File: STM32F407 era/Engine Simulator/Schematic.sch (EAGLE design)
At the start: 23 parts, among them U1 MAX13052ESA+, U2 AD5293BRUZ-100, U3 AD5024BRUZ, X4 057-006-1

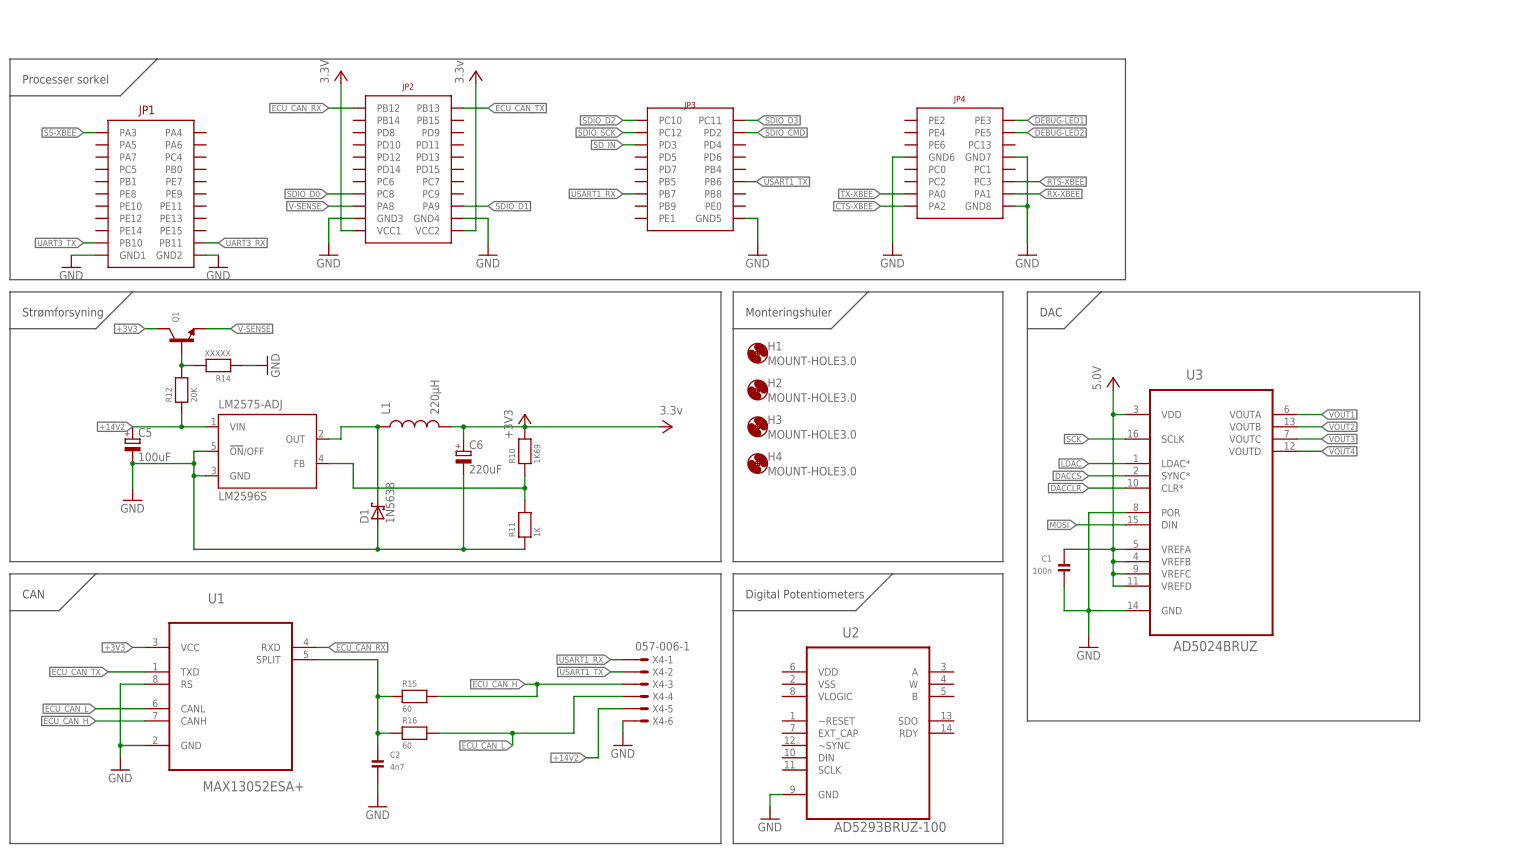
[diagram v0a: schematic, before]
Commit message: DIGITAL POTENTIOMETER
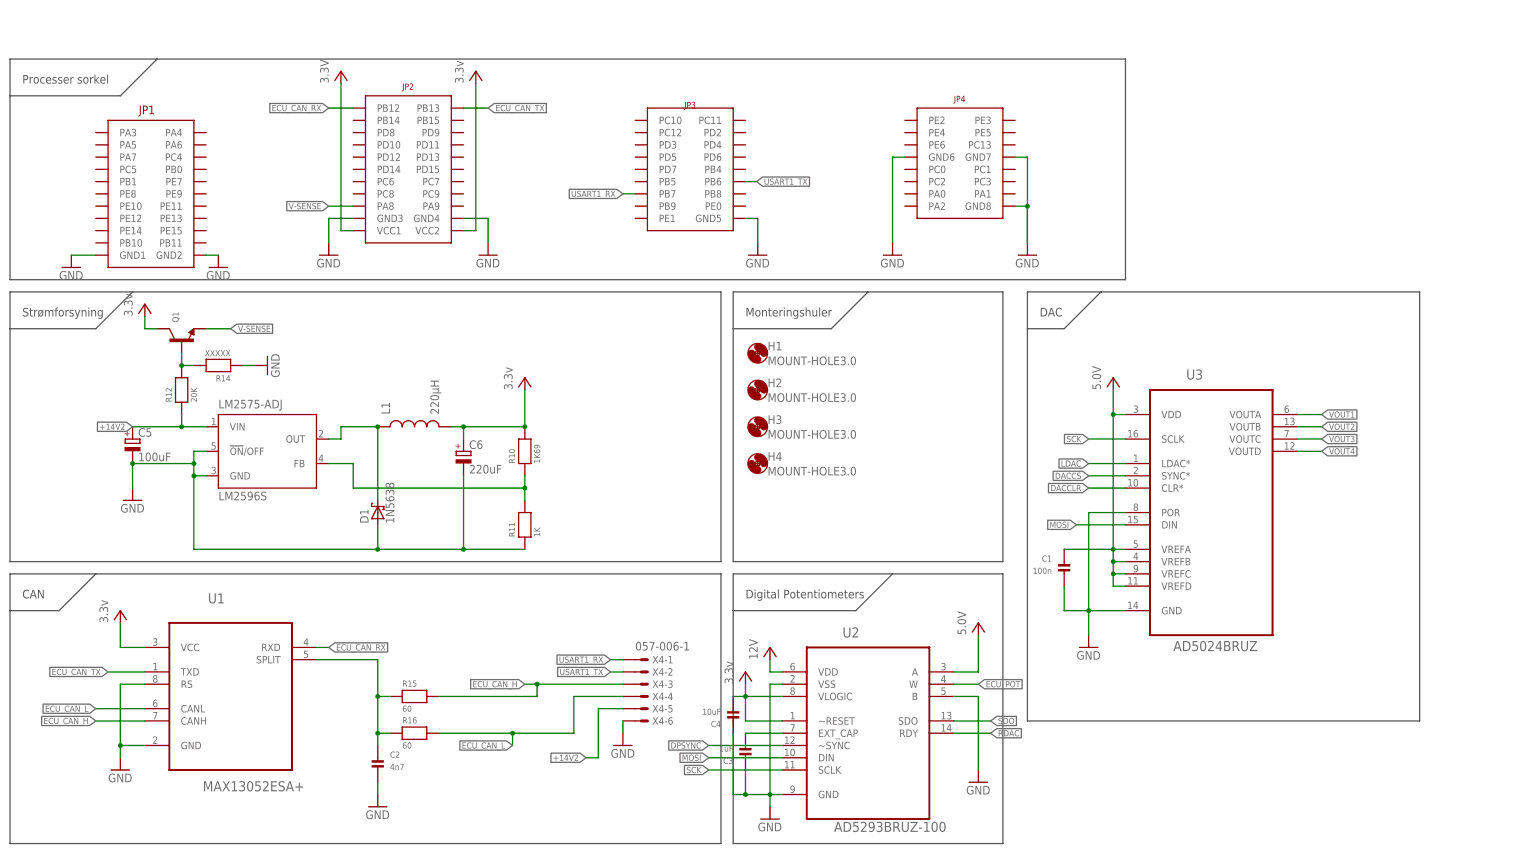
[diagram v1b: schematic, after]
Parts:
- added C3: 1uF, microbuilder:CAP_CERAMIC0603
- added C4: 10uF, microbuilder:CAP_CERAMIC0603
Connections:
- removed net +3V3: C6.+, L1.2, Q1.C, R10.2, U1.VCC
- removed net CTS-XBEE: U$1G$4.PA2
- removed net DEBUG-LED1: U$1G$4.PE3
- removed net DEBUG-LED2: U$1G$4.PE5
- removed net RTS-XBEE: U$1G$4.PC3
- removed net RX-XBEE: U$1G$4.PA1
- removed net SDIO_CMD: U$1G$3.PD2
- removed net SDIO_D0: U$1G$2.PC8
- removed net SDIO_D1: U$1G$2.PA9
- removed net SDIO_D2: U$1G$3.PC10
- removed net SDIO_D3: U$1G$3.PC11
- removed net SDIO_SCK: U$1G$3.PC12
- removed net SD_IN: U$1G$3.PD3
- removed net SS-XBEE: U$1G$1.PA3
- removed net TX-XBEE: U$1G$4.PA0
- removed net UART3_RX: U$1G$1.PB11
- removed net UART3_TX: U$1G$1.PB10
- new net DPSYNC: U2.~SYNC
- new net ECU_POT: U2.W
- new net N$1: C3.P$2, U2.EXT_CAP
- new net RDAC: U2.RDY
- new net SDO: U2.SDO
- net GND: now also C3.P$1, C4.P$1, U2.B, U2.VSS
- net MOSI: now also U2.DIN
- net SCK: now also U2.SCLK
- net VCC: now also C4.P$2, C6.+, L1.2, Q1.C, R10.2, U1.VCC, U2.A, U2.VDD, U2.VLOGIC, U2.~RESET

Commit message: no message
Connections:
- removed net LDAC: U3.LDAC*
- new net SCLK: U$1G$1.PA5, U3.SCLK
- net GND: now also U3.LDAC*
- net MOSI: now also U$1G$3.PB5
- net SCK: no longer U3.SCLK
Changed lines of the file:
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@@
 <net name="USART1_RX" class="0">
+<segment>
+<pinref part="X4" gate="-1" pin="S"/>
+<wire x1="-152.4" y1="-66.04" x2="-149.86" y2="-66.04" width="0.1524" layer="91"/>
+<label x="-152.4" y="-66.04" size="1.27" layer="95" rot="R180" xref="yes"/>
+</segment>
 <segment>
 <pinref part="U$1" gate="G$3" pin="PB7"/>
@@
 <label x="-149.86" y="30.48" size="1.27" layer="95" rot="R180" xref="yes"/>
 </segment>
-<segment>
-<pinref part="X4" gate="-1" pin="S"/>
-<wire x1="-152.4" y1="-66.04" x2="-149.86" y2="-66.04" width="0.1524" layer="91"/>
-<label x="-152.4" y="-66.04" size="1.27" layer="95" rot="R180" xref="yes"/>
-</segment>
 </net>
 <net name="USART1_TX" class="0">
-<segment>
-<pinref part="U$1" gate="G$3" pin="PB6"/>
-<wire x1="-124.46" y1="33.02" x2="-122.174" y2="33.02" width="0.1524" layer="91"/>
-<label x="-122.174" y="33.02" size="1.27" layer="95" xref="yes"/>
-</segment>
 <segment>
 <pinref part="X4" gate="-2" pin="S"/>
 <wire x1="-152.4" y1="-68.58" x2="-149.86" y2="-68.58" width="0.1524" layer="91"/>
 <label x="-152.4" y="-68.58" size="1.27" layer="95" rot="R180" xref="yes"/>
+</segment>
+<segment>
+<pinref part="U$1" gate="G$3" pin="PB6"/>
+<wire x1="-124.46" y1="33.02" x2="-121.92" y2="33.02" width="0.1524" layer="91"/>
+<label x="-121.92" y="33.02" size="1.27" layer="95" xref="yes"/>
 </segment>
 </net>
@@
 <wire x1="-58.42" y1="-50.8" x2="-58.42" y2="-55.88" width="0.1524" layer="91"/>
 <wire x1="-58.42" y1="-55.88" x2="-53.34" y2="-55.88" width="0.1524" layer="91"/>
+<pinref part="U3" gate="A" pin="LDAC*"/>
+<wire x1="-45.72" y1="-25.4" x2="-53.34" y2="-25.4" width="0.1524" layer="91"/>
+<wire x1="-53.34" y1="-25.4" x2="-53.34" y2="-35.56" width="0.1524" layer="91"/>
+<junction x="-53.34" y="-35.56"/>
 </segment>
 <segment>
@@
 <net name="SCK" class="0">
 <segment>
+<pinref part="U2" gate="A" pin="SCLK"/>
+<wire x1="-116.84" y1="-88.9" x2="-132.08" y2="-88.9" width="0.1524" layer="91"/>
+<label x="-132.08" y="-88.9" size="1.27" layer="95" rot="R180" xref="yes"/>
+</segment>
+</net>
+<net name="DACCS" class="0">
+<segment>
+<pinref part="U3" gate="A" pin="SYNC*"/>
+<wire x1="-45.72" y1="-27.94" x2="-55.88" y2="-27.94" width="0.1524" layer="91"/>
+<label x="-55.88" y="-27.94" size="1.27" layer="95" rot="R180" xref="yes"/>
+</segment>
+</net>
+<net name="MOSI" class="0">
+<segment>
+<pinref part="U3" gate="A" pin="DIN"/>
+<wire x1="-45.72" y1="-38.1" x2="-55.88" y2="-38.1" width="0.1524" layer="91"/>
+<label x="-55.88" y="-38.1" size="1.27" layer="95" rot="R180" xref="yes"/>
+</segment>
+<segment>
+<pinref part="U2" gate="A" pin="DIN"/>
+<wire x1="-116.84" y1="-86.36" x2="-132.08" y2="-86.36" width="0.1524" layer="91"/>
+<label x="-132.08" y="-86.36" size="1.27" layer="95" rot="R180" xref="yes"/>
+</segment>
+<segment>
+<pinref part="U$1" gate="G$3" pin="PB5"/>
+<wire x1="-147.32" y1="33.02" x2="-149.86" y2="33.02" width="0.1524" layer="91"/>
+<label x="-149.86" y="33.02" size="1.27" layer="95" rot="R180" xref="yes"/>
+</segment>
+</net>
+<net name="VOUT1" class="0">
+<segment>
+<pinref part="U3" gate="A" pin="VOUTA"/>
+<wire x1="-10.16" y1="-15.24" x2="-5.08" y2="-15.24" width="0.1524" layer="91"/>
+<label x="-5.08" y="-15.24" size="1.27" layer="95" xref="yes"/>
+</segment>
+</net>
+<net name="VOUT2" class="0">
+<segment>
+<pinref part="U3" gate="A" pin="VOUTB"/>
+<wire x1="-10.16" y1="-17.78" x2="-5.08" y2="-17.78" width="0.1524" layer="91"/>
+<label x="-5.08" y="-17.78" size="1.27" layer="95" xref="yes"/>
+</segment>
+</net>
+<net name="VOUT3" class="0">
+<segment>
+<pinref part="U3" gate="A" pin="VOUTC"/>
+<wire x1="-10.16" y1="-20.32" x2="-5.08" y2="-20.32" width="0.1524" layer="91"/>
+<label x="-5.08" y="-20.32" size="1.27" layer="95" xref="yes"/>
+</segment>
+</net>
+<net name="VOUT4" class="0">
+<segment>
+<pinref part="U3" gate="A" pin="VOUTD"/>
+<wire x1="-10.16" y1="-22.86" x2="-5.08" y2="-22.86" width="0.1524" layer="91"/>
+<label x="-5.08" y="-22.86" size="1.27" layer="95" xref="yes"/>
+</segment>
+</net>
+<net name="DACCLR" class="0">
+<segment>
+<pinref part="U3" gate="A" pin="CLR*"/>
+<wire x1="-45.72" y1="-30.48" x2="-55.88" y2="-30.48" width="0.1524" layer="91"/>
+<label x="-55.88" y="-30.48" size="1.27" layer="95" rot="R180" xref="yes"/>
+</segment>
+</net>
+<net name="ECU_POT" class="0">
+<segment>
+<pinref part="U2" gate="A" pin="W"/>
+<wire x1="-81.28" y1="-71.12" x2="-76.2" y2="-71.12" width="0.1524" layer="91"/>
+<label x="-76.2" y="-71.12" size="1.27" layer="95" xref="yes"/>
+</segment>
+</net>
+<net name="N$1" class="0">
+<segment>
+<pinref part="U2" gate="A" pin="EXT_CAP"/>
+<wire x1="-116.84" y1="-81.28" x2="-124.46" y2="-81.28" width="0.1524" layer="91"/>
+<pinref part="C3" gate="G$1" pin="P$2"/>
+</segment>
+</net>
+<net name="DPSYNC" class="0">
+<segment>
+<pinref part="U2" gate="A" pin="~SYNC"/>
+<wire x1="-116.84" y1="-83.82" x2="-132.08" y2="-83.82" width="0.1524" layer="91"/>
+<label x="-132.08" y="-83.82" size="1.27" layer="95" rot="R180" xref="yes"/>
+</segment>
+</net>
+<net name="RDAC" class="0">
+<segment>
+<pinref part="U2" gate="A" pin="RDY"/>
+<wire x1="-81.28" y1="-81.28" x2="-73.66" y2="-81.28" width="0.1524" layer="91"/>
+<label x="-73.66" y="-81.28" size="1.27" layer="95" xref="yes"/>
+</segment>
+</net>
+<net name="SDO" class="0">
+<segment>
+<pinref part="U2" gate="A" pin="SDO"/>
+<wire x1="-81.28" y1="-78.74" x2="-73.66" y2="-78.74" width="0.1524" layer="91"/>
+<label x="-73.66" y="-78.74" size="1.27" layer="95" xref="yes"/>
+</segment>
+</net>
+<net name="SCLK" class="0">
+<segment>
+<pinref part="U$1" gate="G$1" pin="PA5"/>
+<wire x1="-259.08" y1="40.64" x2="-261.62" y2="40.64" width="0.1524" layer="91"/>
+<label x="-261.62" y="40.64" size="1.27" layer="95" rot="R180" xref="yes"/>
+</segment>
+<segment>
 <pinref part="U3" gate="A" pin="SCLK"/>
 <wire x1="-45.72" y1="-20.32" x2="-53.34" y2="-20.32" width="0.1524" layer="91"/>
 <label x="-53.34" y="-20.32" size="1.27" layer="95" rot="R180" xref="yes"/>
 </segment>
-<segment>
-<pinref part="U2" gate="A" pin="SCLK"/>
-<wire x1="-116.84" y1="-88.9" x2="-132.08" y2="-88.9" width="0.1524" layer="91"/>
-<label x="-132.08" y="-88.9" size="1.27" layer="95" rot="R180" xref="yes"/>
-</segment>
-</net>
-<net name="LDAC" class="0">
-<segment>
-<pinref part="U3" gate="A" pin="LDAC*"/>
-<wire x1="-45.72" y1="-25.4" x2="-53.34" y2="-25.4" width="0.1524" layer="91"/>
-<label x="-53.34" y="-25.4" size="1.27" layer="95" rot="R180" xref="yes"/>
-</segment>
-</net>
-<net name="DACCS" class="0">
-<segment>
-<pinref part="U3" gate="A" pin="SYNC*"/>
-<wire x1="-45.72" y1="-27.94" x2="-53.34" y2="-27.94" width="0.1524" layer="91"/>
-<label x="-53.34" y="-27.94" size="1.27" layer="95" rot="R180" xref="yes"/>
-</segment>
-</net>
-<net name="MOSI" class="0">
-<segment>
-<pinref part="U3" gate="A" pin="DIN"/>
-<wire x1="-45.72" y1="-38.1" x2="-55.88" y2="-38.1" width="0.1524" layer="91"/>
-<label x="-55.88" y="-38.1" size="1.27" layer="95" rot="R180" xref="yes"/>
-</segment>
-<segment>
-<pinref part="U2" gate="A" pin="DIN"/>
-<wire x1="-116.84" y1="-86.36" x2="-132.08" y2="-86.36" width="0.1524" layer="91"/>
-<label x="-132.08" y="-86.36" size="1.27" layer="95" rot="R180" xref="yes"/>
-</segment>
-</net>
-<net name="VOUT1" class="0">
-<segment>
-<pinref part="U3" gate="A" pin="VOUTA"/>
-<wire x1="-10.16" y1="-15.24" x2="-5.08" y2="-15.24" width="0.1524" layer="91"/>
-<label x="-5.08" y="-15.24" size="1.27" layer="95" xref="yes"/>
-</segment>
-</net>
-<net name="VOUT2" class="0">
-<segment>
-<pinref part="U3" gate="A" pin="VOUTB"/>
-<wire x1="-10.16" y1="-17.78" x2="-5.08" y2="-17.78" width="0.1524" layer="91"/>
-<label x="-5.08" y="-17.78" size="1.27" layer="95" xref="yes"/>
-</segment>
-</net>
-<net name="VOUT3" class="0">
-<segment>
-<pinref part="U3" gate="A" pin="VOUTC"/>
-<wire x1="-10.16" y1="-20.32" x2="-5.08" y2="-20.32" width="0.1524" layer="91"/>
-<label x="-5.08" y="-20.32" size="1.27" layer="95" xref="yes"/>
-</segment>
-</net>
-<net name="VOUT4" class="0">
-<segment>
-<pinref part="U3" gate="A" pin="VOUTD"/>
-<wire x1="-10.16" y1="-22.86" x2="-5.08" y2="-22.86" width="0.1524" layer="91"/>
-<label x="-5.08" y="-22.86" size="1.27" layer="95" xref="yes"/>
-</segment>
-</net>
-<net name="DACCLR" class="0">
-<segment>
-<pinref part="U3" gate="A" pin="CLR*"/>
-<wire x1="-45.72" y1="-30.48" x2="-53.34" y2="-30.48" width="0.1524" layer="91"/>
-<label x="-53.34" y="-30.48" size="1.27" layer="95" rot="R180" xref="yes"/>
-</segment>
-</net>
-<net name="ECU_POT" class="0">
-<segment>
-<pinref part="U2" gate="A" pin="W"/>
-<wire x1="-81.28" y1="-71.12" x2="-76.2" y2="-71.12" width="0.1524" layer="91"/>
-<label x="-76.2" y="-71.12" size="1.27" layer="95" xref="yes"/>
-</segment>
-</net>
-<net name="N$1" class="0">
-<segment>
-<pinref part="U2" gate="A" pin="EXT_CAP"/>
-<wire x1="-116.84" y1="-81.28" x2="-124.46" y2="-81.28" width="0.1524" layer="91"/>
-<pinref part="C3" gate="G$1" pin="P$2"/>
-</segment>
-</net>
-<net name="DPSYNC" class="0">
-<segment>
-<pinref part="U2" gate="A" pin="~SYNC"/>
-<wire x1="-116.84" y1="-83.82" x2="-132.08" y2="-83.82" width="0.1524" layer="91"/>
-<label x="-132.08" y="-83.82" size="1.27" layer="95" rot="R180" xref="yes"/>
-</segment>
-</net>
-<net name="RDAC" class="0">
-<segment>
-<pinref part="U2" gate="A" pin="RDY"/>
-<wire x1="-81.28" y1="-81.28" x2="-73.66" y2="-81.28" width="0.1524" layer="91"/>
-<label x="-73.66" y="-81.28" size="1.27" layer="95" xref="yes"/>
-</segment>
-</net>
-<net name="SDO" class="0">
-<segment>
-<pinref part="U2" gate="A" pin="SDO"/>
-<wire x1="-81.28" y1="-78.74" x2="-73.66" y2="-78.74" width="0.1524" layer="91"/>
-<label x="-73.66" y="-78.74" size="1.27" layer="95" xref="yes"/>
-</segment>
-</net>
+</net>

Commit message: no message
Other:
- moved on the sheet: C3, C4, U2
